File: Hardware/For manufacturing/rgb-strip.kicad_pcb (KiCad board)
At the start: 2 copper layers, 18 parts, among them IC1 ATTINY84-P, K1 PIXEL, P1 BT_Header-1x06, P2 FAN, Q1 HC49, SW1 RST, U1 7805SRH-C, U2 ICSP

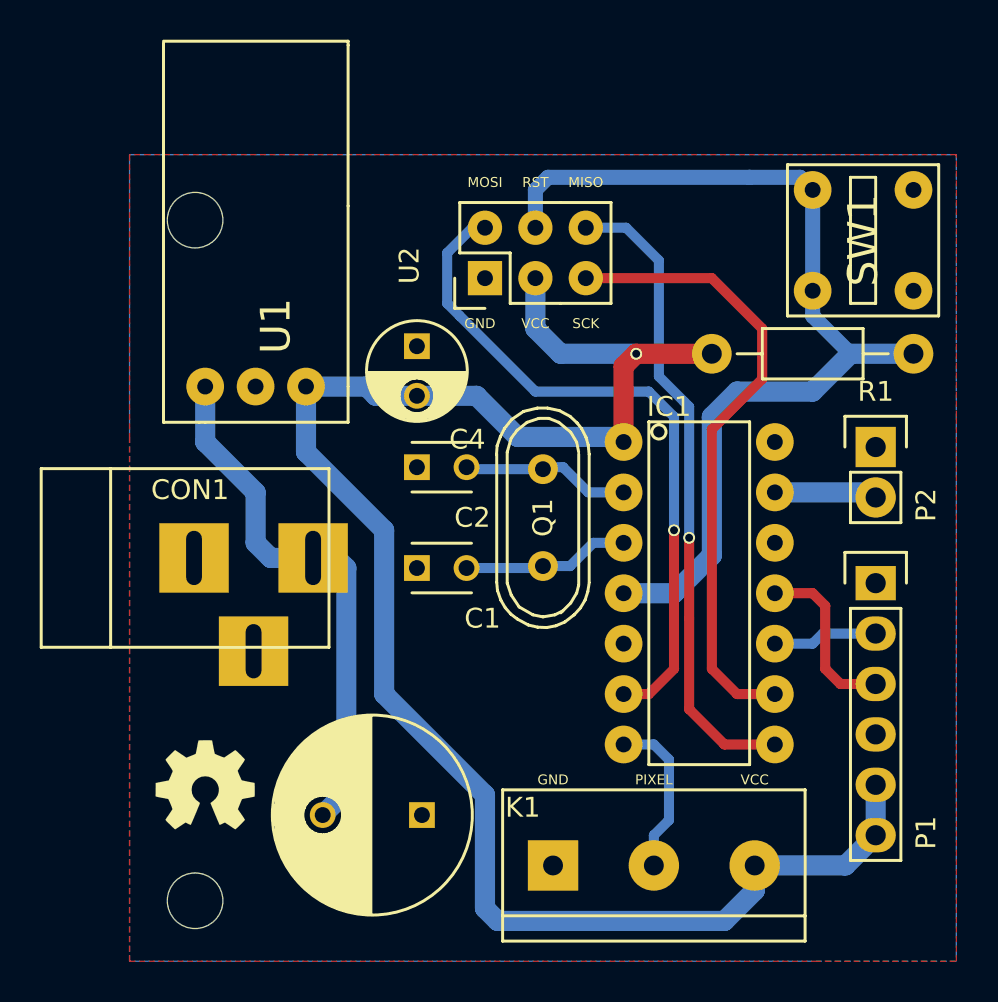
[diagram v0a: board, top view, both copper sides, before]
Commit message: Finished board - minor improvements - Removed fan support
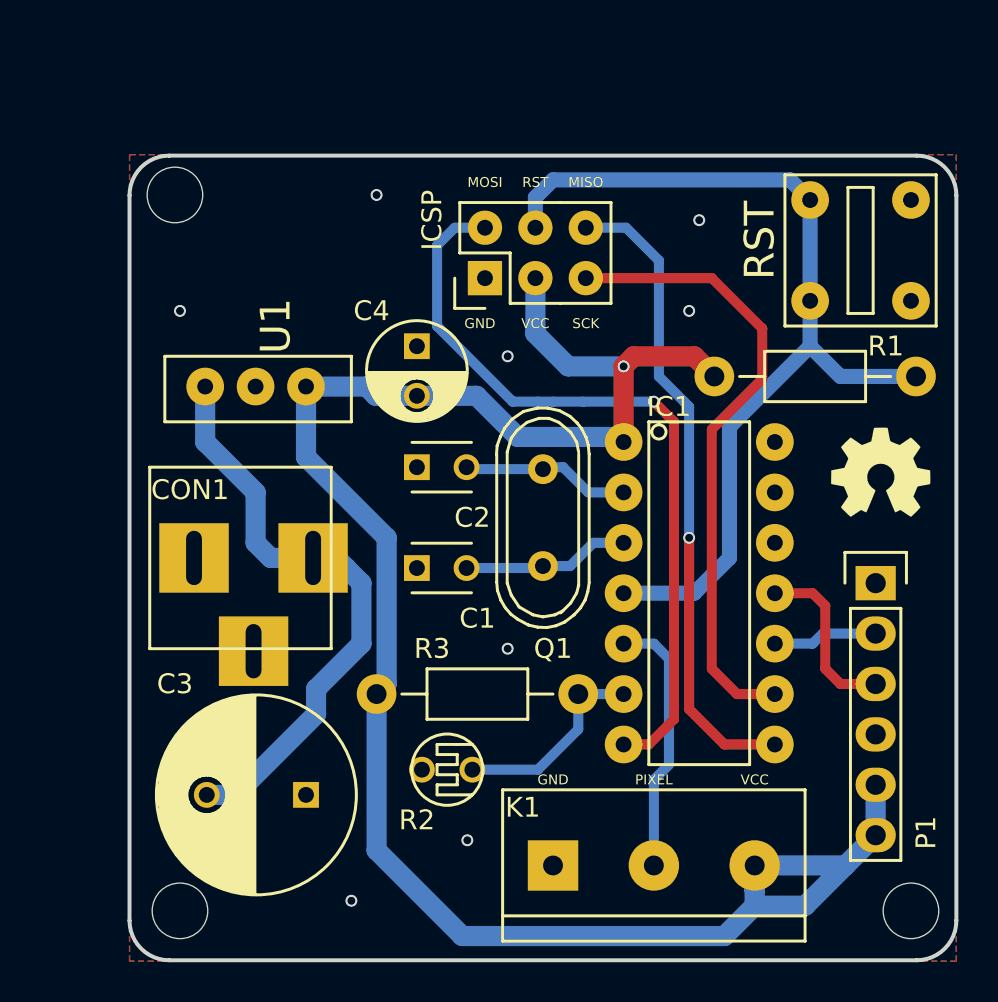
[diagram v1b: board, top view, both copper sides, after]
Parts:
- removed the ? at (72.4, 108.2)
- removed the ? at (72.4, 73.9)
- removed LOGO_OSHW_silkscreen_5mm: val**, library:LOGO_OSHW_B.SilkS_5mm
- removed P2: FAN, Pin_Headers:Pin_Header_Straight_1x02
- removed SW1: RST, library:SW_PUSH
- added ?: MountingHole_2-7mm, library:MountingHole_2-8mm, F.Cu at (71.6, 108.7)
- added ?: MountingHole_2-7mm, library:MountingHole_2-8mm, F.Cu at (71.4, 72.6)
- added ?: val**, library:LOGO_OSHW_B.SilkS_5mm, B.SilkS at (106.9, 86.6)
- added ?: MountingHole_2-7mm, library:MountingHole_2-8mm, F.Cu at (108.5, 108.7)
- added R2: LDR, library:LDR, F.Cu at (86.4, 101.6)
- added R3: 10K, Resistors_ThroughHole:Resistor_Horizontal_RM10mm, F.Cu at (86.6, 97.8)
- added RST: SW_PUSH, library:SW_PUSH, F.Cu at (103.4, 72.9)
- ?: value (none) -> val**
- CON1: value (none) -> BARREL_JACK
- K1: value PIXEL -> CONN_3_V
- U1: value 7805SRH-C -> 7805
- moved ? 37.5 mm to (106.9, 86.6)
- moved C3 5.93 mm to (78.0, 102.9)
- moved R1 1.15 mm to (103.6, 81.8)
- renumbered U2 to ICSP
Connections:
- IC1 pad 13: FAN -> Net-(IC1-Pad13)
- IC1 pad 5: Net-(IC1-Pad5) -> PixelPin
- IC1 pad 6: MOSI -> LDR
- IC1 pad 7: PixelPin -> MOSI
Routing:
- net LDR: track 0.00 -> 10.2 mm
- net VCC: track 88.9 -> 98.8 mm
- net FAN: track 5.54 -> 0.00 mm
- net PixelPin: track 8.25 -> 13.3 mm
- net MOSI: track 35.2 -> 40.1 mm
- net Net-(C3-Pad2): track 28.0 -> 32.7 mm
- net RST: track 49.1 -> 47.9 mm
- net (no net): vias 0 -> 8
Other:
- board outline added: 41.7 x 40.5 mm

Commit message: Improved design and updated gerbers
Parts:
- removed RST: SW_PUSH, library:SW_PUSH
- added SW1: SW_PUSH, library:SW_PUSH, F.Cu at (103.4, 73.2)
- moved ICSP 2.01 mm to (94.0, 74.9)
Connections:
- ICSP pad 1: MISO -> GND
- ICSP pad 2: SCK -> RST
- ICSP pad 3: RST -> MOSI
- ICSP pad 4: VCC -> SCK
- ICSP pad 5: MOSI -> VCC
- ICSP pad 6: GND -> MISO
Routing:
- net VCC: track 98.8 -> 107.8 mm, vias 1 -> 0
- net RST: track 47.9 -> 41.5 mm
- net SCK: track 31.8 -> 28.4 mm, vias 0 -> 1
- net MOSI: track 40.1 -> 40.5 mm, vias 1 -> 0
- net (no net): vias 8 -> 6
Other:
- board text added: "MISO"
- board text added: "MOSI"
- board text added: "RST"
- board text added: "SCK"
- board text added: "Vcc"
